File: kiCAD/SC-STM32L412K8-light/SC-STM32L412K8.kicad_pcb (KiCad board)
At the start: 2 copper layers, 31.6 x 15.1 mm, 67 parts, among them J1 usb, J11 Vibro, J12 +3v, J13 +vibro, J14 gndBT, J15 -BAT, J2 +29.6 SiPM, J3 TxD (20), J4 RxD (19), J5 SWDIO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

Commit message: изменено:      kiCAD/SC-STM32L412K8-light/SC-STM32L412K8-rescue.lib 	изменено:      kiCAD/SC-STM32L412K8-light/SC-STM32L412K8.kicad_pcb
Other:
- net class Default removed

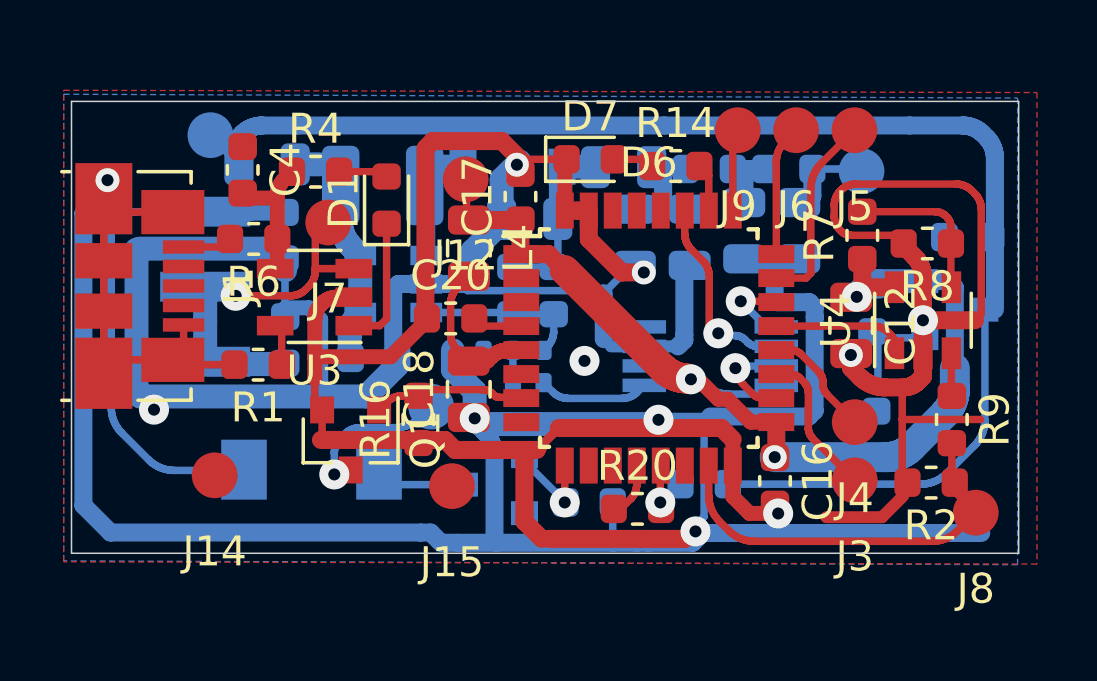
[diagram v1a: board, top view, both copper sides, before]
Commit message: изменено:      kiCAD/SC-STM32L412K8-light/SC-STM32L412K8.kicad_pcb 	изменено:      kiCAD/SC-STM32L412K8-light/fp-info-cache 	kiCAD/SC-STM32L412K8-light/SC-STM32L412K8-job.gbrjob 	kiCAD/SC-STM32L412K8-light/SC-STM32L412K8.kicad_prl 	kiCAD/SC-STM32L412K8-light/SC-STM32L412K8.kicad_pro 	kiCAD/SC-STM32L412K8-light/SC-STM32L412K8.kicad_sch
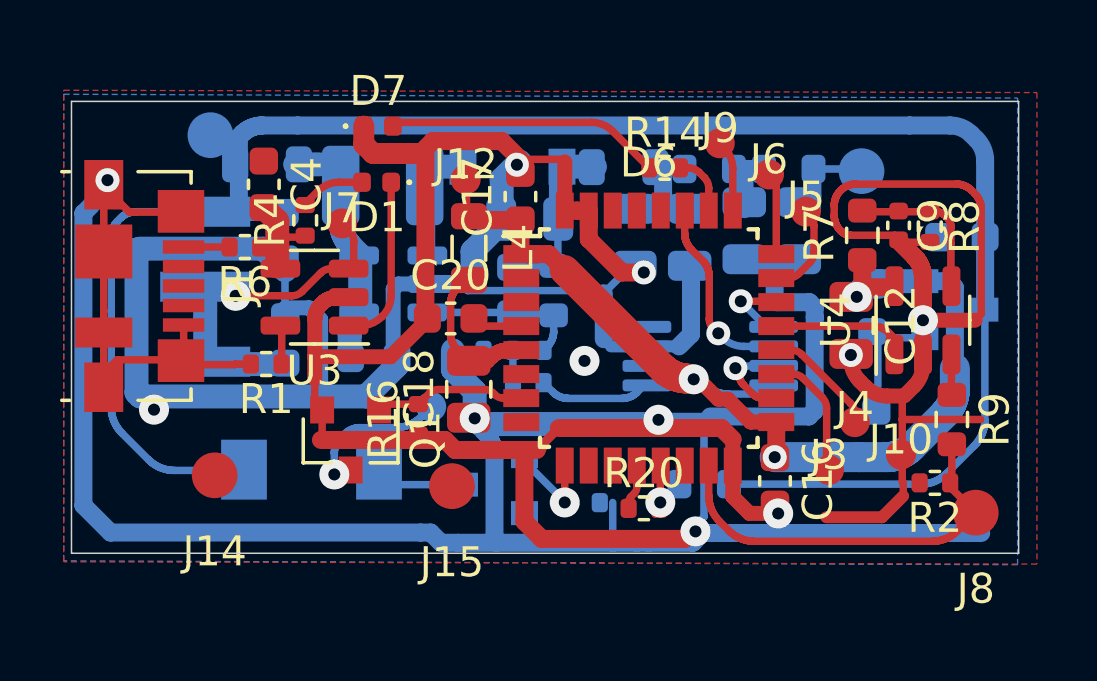
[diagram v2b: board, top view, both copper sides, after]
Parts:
- added C9: 10n, Capacitor_SMD:C_0402_1005Metric, F.Cu at (55.0, 57.0)
- added J10: gnd, lib:conn_mini, F.Cu at (55.1, 64.7)
- D1, D7: footprint LED_SMD:LED_0603_1608Metric -> LED_SMD:LED_0402_1005Metric
- J11, J12, J3, J4, J5, J6, J7, J9: footprint My-library:SMD-CONN -> lib:conn_mini
- R1, R14, R15, R16, R2, R20, R4, R6, R8: footprint Resistor_SMD:R_0603_1608Metric -> Resistor_SMD:R_0402_1005Metric
- moved D7 7.15 mm to (37.7, 53.7)
- moved J5 3.16 mm to (51.9, 56.5)
- moved J6 1.73 mm to (50.7, 55.3)
- moved R4 1.66 mm to (35.2, 56.8), turned to 90 degrees
- moved J3 0.93 mm to (52.7, 65.2)
- moved C4 0.85 mm to (33.9, 55.6)
- moved J9 0.74 mm to (49.1, 54.3)
- moved D1 0.68 mm to (37.6, 55.6), turned to 180 degrees
- moved R8 0.57 mm to (56.1, 57.0), turned to -90 degrees
- moved J7 0.46 mm to (36.5, 56.9)
- moved R6 0.40 mm to (33.2, 57.7)
- moved R14 0.38 mm to (47.2, 55.1)
- moved R1 0.27 mm to (33.9, 61.6)
- moved R20 0.22 mm to (46.5, 66.4)
- moved C15 0.20 mm to (57.1, 57.4)
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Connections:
- D3 pad 8: (no net) -> unconnected-(D3-Pad8)
- D6 pad 10: (no net) -> unconnected-(D6-Pad10)
- D6 pad 11: (no net) -> unconnected-(D6-Pad11)
- D6 pad 14: (no net) -> unconnected-(D6-Pad14)
- D6 pad 2: (no net) -> unconnected-(D6-Pad2)
- D6 pad 28: (no net) -> unconnected-(D6-Pad28)
- D6 pad 29: (no net) -> unconnected-(D6-Pad29)
- D6 pad 3: (no net) -> unconnected-(D6-Pad3)
- D6 pad 30: (no net) -> unconnected-(D6-Pad30)
- D6 pad 6: (no net) -> unconnected-(D6-Pad6)
- D6 pad 8: (no net) -> unconnected-(D6-Pad8)
- J1 pad 2: (no net) -> unconnected-(J1-Pad2)
- J1 pad 3: (no net) -> unconnected-(J1-Pad3)
- J1 pad 4: (no net) -> unconnected-(J1-Pad4)
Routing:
- net Net-(D7-Pad2): track 1.22 -> 9.18 mm
- net GND: track 221.6 -> 225.7 mm
- net Net-(D6-Pad23): track 6.54 -> 3.13 mm
- net Net-(D6-Pad24): track 4.36 -> 2.75 mm
- net Net-(D1-Pad1): track 4.21 -> 5.57 mm
- net Net-(C4-Pad2): track 4.59 -> 3.69 mm
- net Net-(D1-Pad2): track 1.58 -> 2.27 mm
- net +BATT: track 66.5 -> 65.9 mm
- net Net-(D6-Pad19): track 4.95 -> 4.32 mm
